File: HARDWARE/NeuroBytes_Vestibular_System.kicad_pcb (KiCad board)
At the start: 2 copper layers, 52.3 x 46.4 mm, 50 parts, among them P1 JST GH 4-POS, P2 JST GH 4-POS, P5 JST GH 4-POS, P6 JST GH 4-POS, P7 JST GH 4-POS, P8 JST GH 7-POS, Q1 NPN_dual, Q2 NPN_dual, SW1 SW_PUSH_TL3330AF130QG, U1 STM32L011Gx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

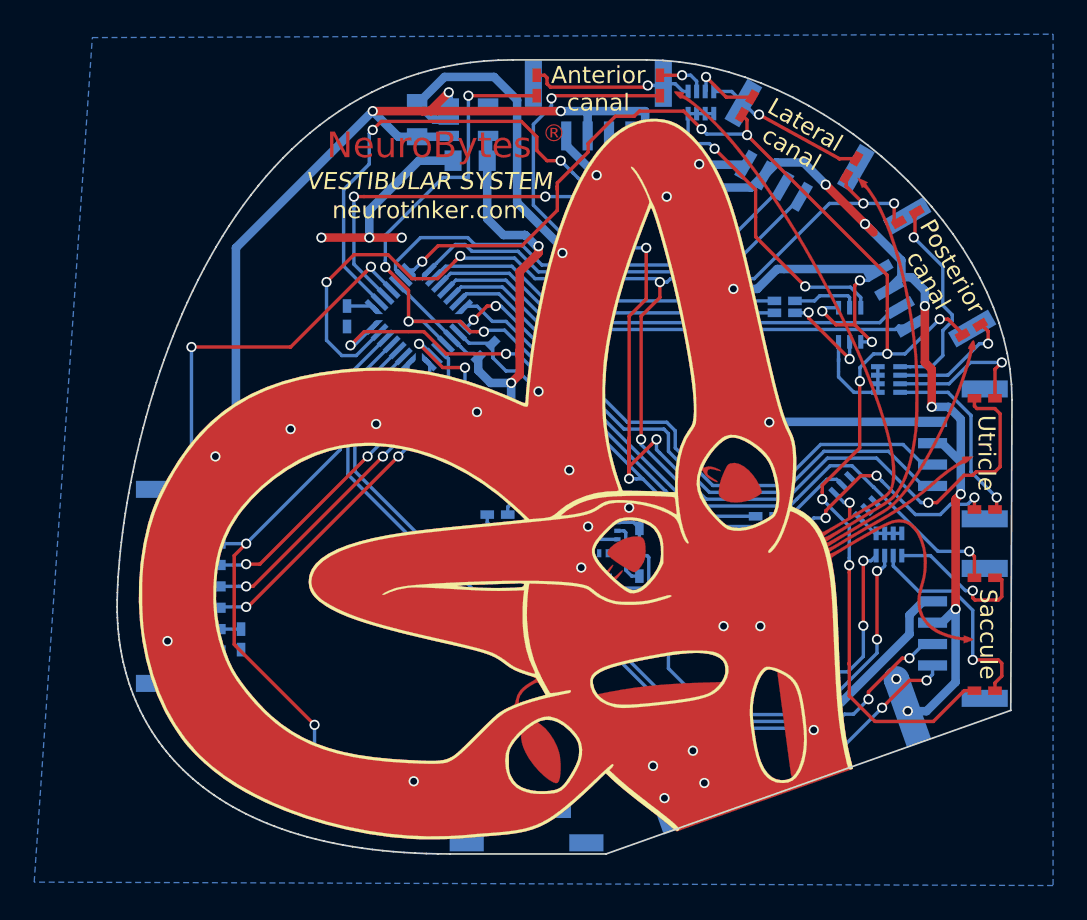
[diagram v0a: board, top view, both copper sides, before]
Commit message: reversed LEDs
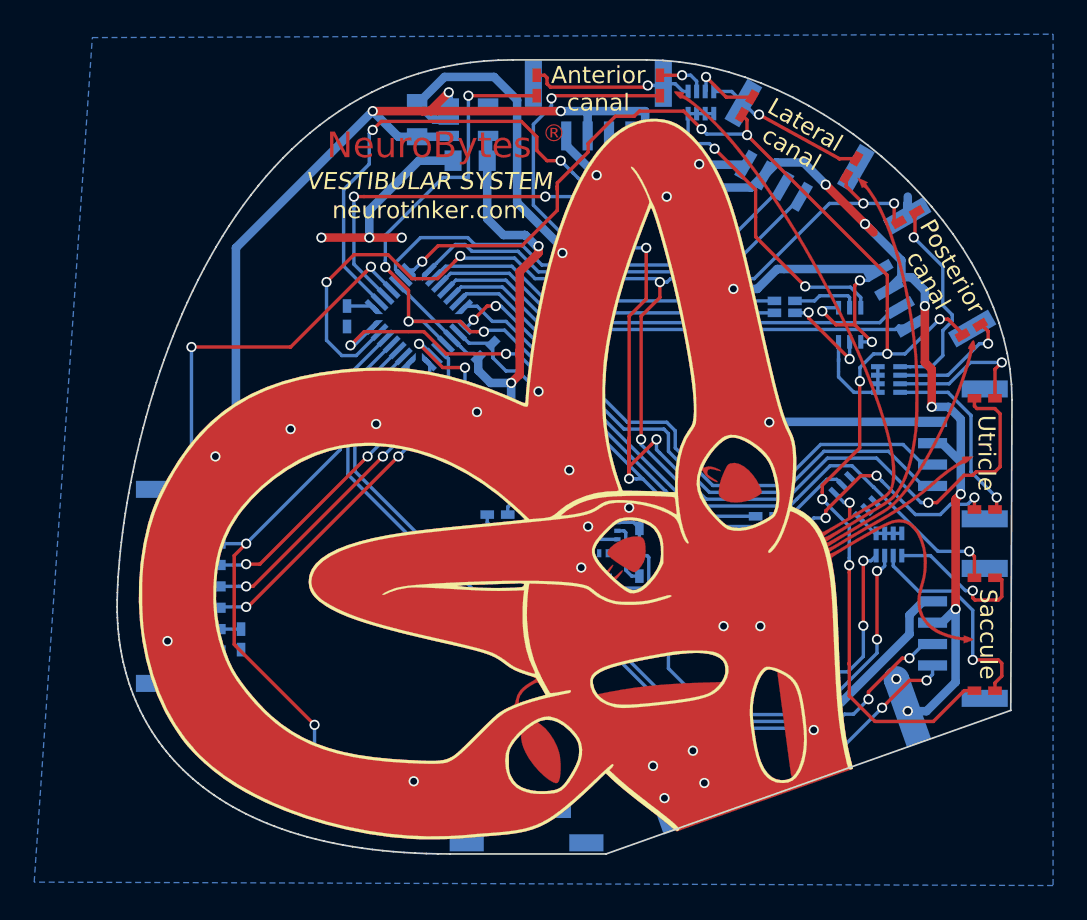
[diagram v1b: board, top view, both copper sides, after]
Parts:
- turned D1 to 270 degrees
- turned D10 to 180 degrees
- turned D11 to 90 degrees
- turned D12 to 90 degrees
- turned D2 to 210 degrees
- turned D3 to 270 degrees
- turned D4 to 210 degrees
- turned D5 to 240 degrees
- turned D6 to 240 degrees
- turned D7 to 180 degrees
- turned D8 to 180 degrees
- turned D9 to 180 degrees
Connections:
- D1 pad 1: LED_X0 -> Net-(D1-Pad1)
- D1 pad 2: Net-(D1-Pad2) -> LED_X0
- D10 pad 1: LED_X2 -> Net-(D10-Pad1)
- D10 pad 2: Net-(D10-Pad2) -> LED_X2
- D11 pad 1: LED_X0 -> Net-(D11-Pad1)
- D11 pad 2: Net-(D11-Pad2) -> LED_X0
- D12 pad 1: LED_X1 -> Net-(D12-Pad1)
- D12 pad 2: Net-(D12-Pad2) -> LED_X1
- D2 pad 1: LED_X3 -> Net-(D2-Pad1)
- D2 pad 2: Net-(D2-Pad2) -> LED_X3
- D3 pad 1: LED_X1 -> Net-(D3-Pad1)
- D3 pad 2: Net-(D3-Pad2) -> LED_X1
- D4 pad 1: LED_X2 -> Net-(D4-Pad1)
- D4 pad 2: Net-(D4-Pad2) -> LED_X2
- D5 pad 1: LED_X2 -> Net-(D5-Pad1)
- D5 pad 2: Net-(D5-Pad2) -> LED_X2
- D6 pad 1: LED_X3 -> Net-(D6-Pad1)
- D6 pad 2: Net-(D6-Pad2) -> LED_X3
- D7 pad 1: LED_X1 -> Net-(D7-Pad1)
- D7 pad 2: Net-(D7-Pad2) -> LED_X1
- D8 pad 1: LED_X0 -> Net-(D8-Pad1)
- D8 pad 2: Net-(D8-Pad2) -> LED_X0
- D9 pad 1: LED_X3 -> Net-(D9-Pad1)
- D9 pad 2: Net-(D9-Pad2) -> LED_X3
- P1 pad : (no net) -> GND
- P2 pad : (no net) -> GND
- P5 pad : (no net) -> Net-(D6-Pad1)
- P6 pad : (no net) -> GND
- P7 pad : (no net) -> GND
- P8 pad : (no net) -> GND
- RN1 pad 5: Net-(D6-Pad2) -> Net-(D6-Pad1)
- RN1 pad 6: Net-(D5-Pad2) -> Net-(D5-Pad1)
- RN1 pad 7: Net-(D3-Pad2) -> Net-(D3-Pad1)
- RN1 pad 8: Net-(D1-Pad2) -> Net-(D1-Pad1)
- RN3 pad 5: Net-(D8-Pad2) -> Net-(D8-Pad1)
- RN3 pad 6: Net-(D7-Pad2) -> Net-(D7-Pad1)
- RN3 pad 7: Net-(D4-Pad2) -> Net-(D4-Pad1)
- RN3 pad 8: Net-(D2-Pad2) -> Net-(D2-Pad1)
- RN4 pad 5: Net-(D11-Pad2) -> Net-(D11-Pad1)
- RN4 pad 6: Net-(D12-Pad2) -> Net-(D12-Pad1)
- RN4 pad 7: Net-(D10-Pad2) -> Net-(D10-Pad1)
- RN4 pad 8: Net-(D9-Pad2) -> Net-(D9-Pad1)
- SW1 pad : (no net) -> GND
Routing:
- net Net-(D12-Pad2): track 22.6 -> 0.00 mm, vias 2 -> 0
- net Net-(D12-Pad1): track 0.00 -> 22.6 mm, vias 0 -> 2
- net Net-(D10-Pad2): track 12.8 -> 0.00 mm, vias 1 -> 0
- net Net-(D10-Pad1): track 0.00 -> 12.8 mm, vias 0 -> 1
- net Net-(D2-Pad2): track 12.3 -> 0.00 mm, vias 1 -> 0
- net Net-(D2-Pad1): track 0.00 -> 12.3 mm, vias 0 -> 1
- net Net-(D11-Pad2): track 11.4 -> 0.00 mm, vias 2 -> 0
- net Net-(D11-Pad1): track 0.00 -> 11.4 mm, vias 0 -> 2
- net Net-(D8-Pad2): track 10.9 -> 0.00 mm, vias 1 -> 0
- net Net-(D8-Pad1): track 0.00 -> 10.9 mm, vias 0 -> 1
- net Net-(D6-Pad2): track 9.62 -> 0.00 mm, vias 1 -> 0
- net Net-(D6-Pad1): track 0.00 -> 9.62 mm, vias 0 -> 1
- net Net-(D1-Pad2): track 9.61 -> 0.00 mm, vias 1 -> 0
- net Net-(D1-Pad1): track 0.00 -> 9.61 mm, vias 0 -> 1
- net Net-(D7-Pad2): track 8.88 -> 0.00 mm, vias 1 -> 0
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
